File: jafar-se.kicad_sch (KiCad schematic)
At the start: 15 parts, among them J1 XBOX LPC, J2 JTAG, J3 D0 (1.0-1.4), U1 LC4032V-75TN44I, U2 SST49LF080A-33-4C-NHE

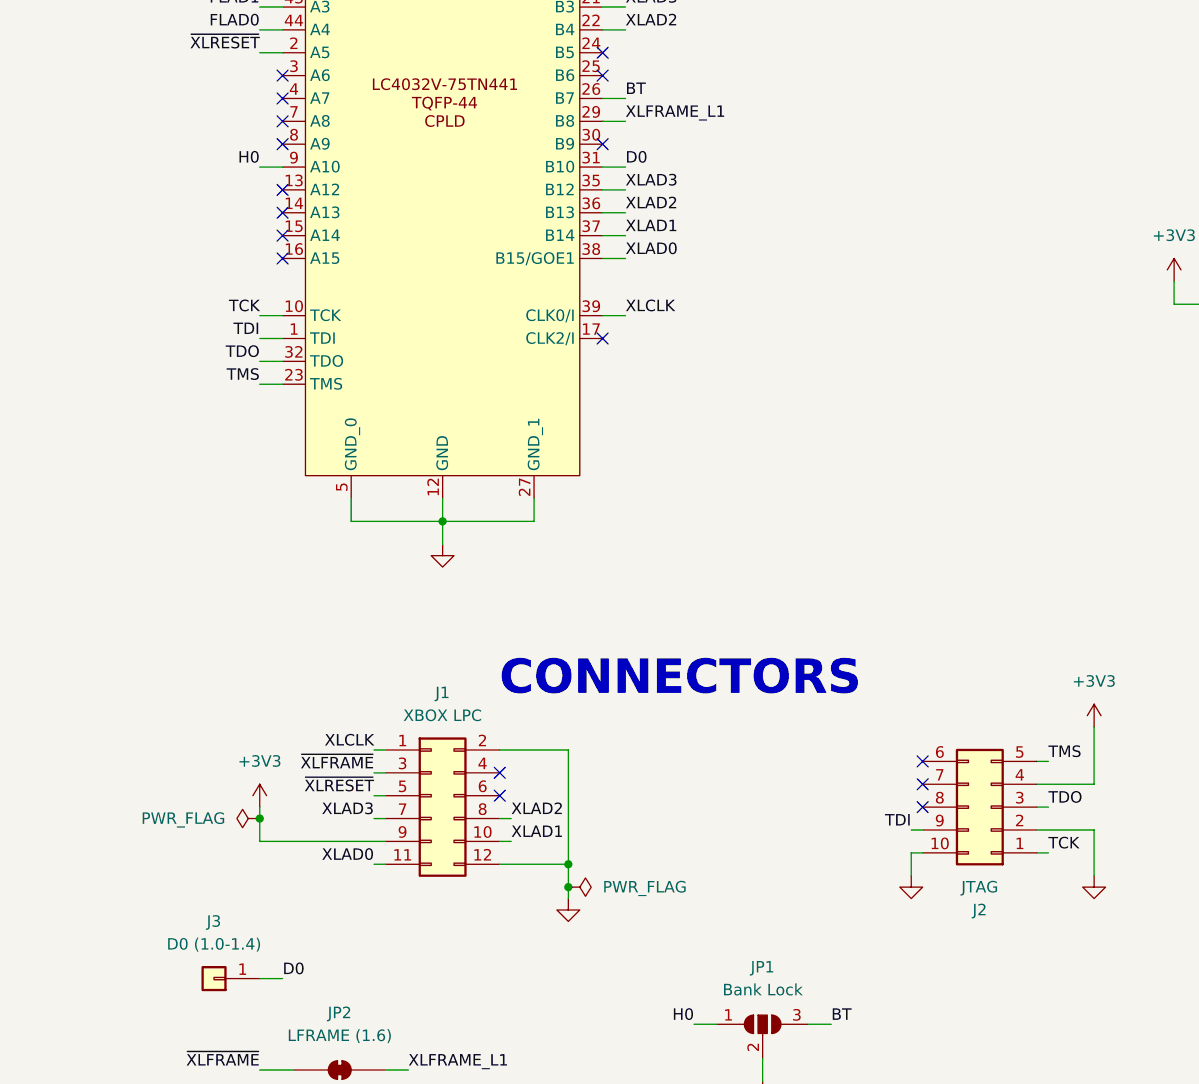
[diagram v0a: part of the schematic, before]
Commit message: Moved pads and rerouted
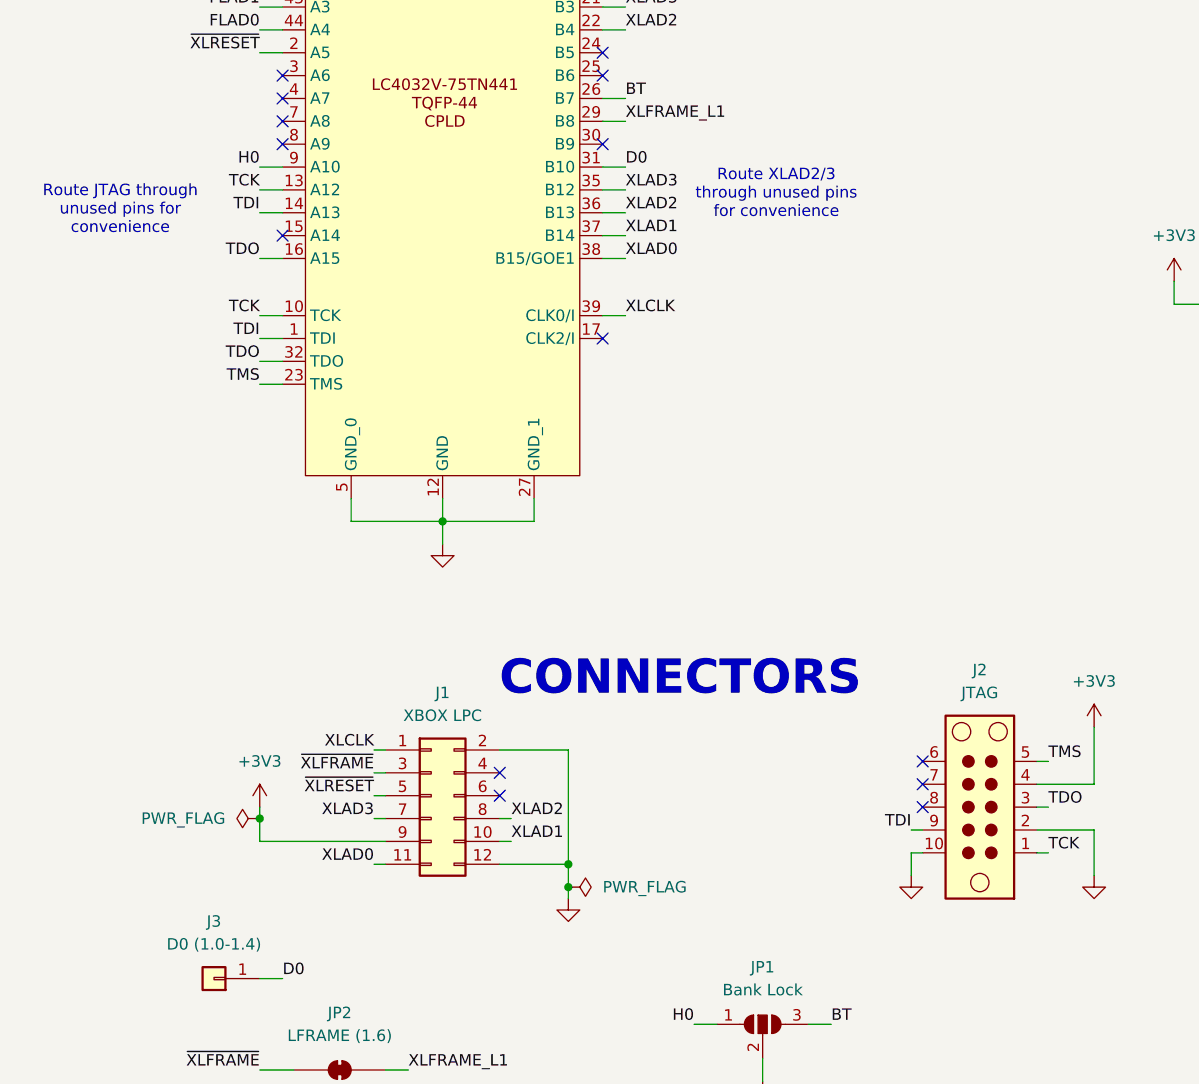
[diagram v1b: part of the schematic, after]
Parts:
- removed J2: JTAG, Connector:Tag-Connect_TC2050-IDC-NL_2x05_P1.27mm_Vertical, symbol Connector_Generic:Conn_02x05_Counter_Clockwise
- added J2: JTAG, Connector:Tag-Connect_TC2050-IDC-NL_2x05_P1.27mm_Vertical, symbol Connector:TC2050
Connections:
- net +3V3: now also J2.4
- net GND: now also J2.10, J2.2
- net TCK: now also U1.13 (A12), J2.1
- net TDI: now also U1.14 (A13), J2.9
- net TDO: now also U1.16 (A15), J2.3
- net TMS: now also J2.5
- no-connect marks 24 -> 21
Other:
- note added: "Route JTAG through unused pins for convenience"
- note added: "Route XLAD2/3 through unused pins for convenience"
